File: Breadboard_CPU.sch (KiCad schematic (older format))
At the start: 20 parts, among them Q5 Q_NPN_CBE, SW3 RESET

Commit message: Pre non-interrupt split
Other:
- moved on the sheet: D14, D15, D16, D17, D18, D19, D20, D21, Q5, R100, R101, R102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

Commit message: Replaced all broken schematics with the up-to-date versions.  Some symbols missing.  This version will be the one created IRL except for the carry flag.
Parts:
- added R110: 10k, symbol Breadboard_CPU-rescue:R-Device
- D101: renamed from D14; symbol Device:LED -> Breadboard_CPU-rescue:LED-Device
- D102: renamed from D15; symbol Device:LED -> Breadboard_CPU-rescue:LED-Device
- D103: renamed from D16; symbol Device:LED -> Breadboard_CPU-rescue:LED-Device
- D104: renamed from D17; symbol Device:LED -> Breadboard_CPU-rescue:LED-Device
- D105: renamed from D18; symbol Device:LED -> Breadboard_CPU-rescue:LED-Device
- D106: renamed from D19; symbol Device:LED -> Breadboard_CPU-rescue:LED-Device
- D107: renamed from D20; symbol Device:LED -> Breadboard_CPU-rescue:LED-Device
- D108: renamed from D21; symbol Device:LED -> Breadboard_CPU-rescue:LED-Device
- Q101: renamed from Q5; value Q_NPN_CBE -> 2N2222; symbol Device:Q_NPN_CBE -> Breadboard_CPU-rescue:Q_NPN_CBE-Device
- R101: renamed from R99; symbol Device:R -> Breadboard_CPU-rescue:R-Device
- R102: renamed from R100; symbol Device:R -> Breadboard_CPU-rescue:R-Device
- R103: renamed from R101; symbol Device:R -> Breadboard_CPU-rescue:R-Device
- R104: renamed from R102; symbol Device:R -> Breadboard_CPU-rescue:R-Device
- R105: renamed from R103; symbol Device:R -> Breadboard_CPU-rescue:R-Device
- R106: renamed from R104; symbol Device:R -> Breadboard_CPU-rescue:R-Device
- R107: renamed from R105; symbol Device:R -> Breadboard_CPU-rescue:R-Device
- R108: renamed from R106; symbol Device:R -> Breadboard_CPU-rescue:R-Device
- R109: renamed from R29; symbol Device:R -> Breadboard_CPU-rescue:R-Device
- R111: renamed from R30; symbol Device:R -> Breadboard_CPU-rescue:R-Device
- SW101: renamed from SW3; symbol Switch:SW_Push -> Breadboard_CPU-rescue:SW_Push-Switch
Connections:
- net Clock Module/HALT_C renamed RST
- net RST: now also R110.1; no longer Q101.2 (B)
- net Control Unit Module/~RST renamed ~RST
- new net: Q101.2 (B), R110.2
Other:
- note added: "Annotation Key:\n100's: Main Sheet\n200's: Power Module\n300's: Clock Module\n400's: Memory Module\n500's: ALU Module\n600's: Control Unit\n700's: Registers Module\n800's PC Module"
- moved on the sheet: D101, D102, D103, D104, D105, D106, D107, D108, R101, R102, R103, R104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

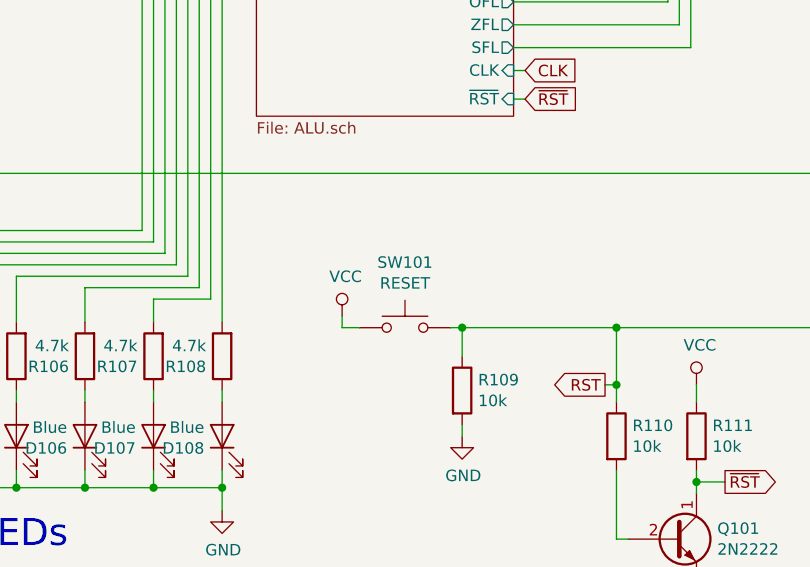
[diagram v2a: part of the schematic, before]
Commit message: Fixed CFL timing violation bug.  TOFIX: move away from rescue .lib symbols and fix the 2x 4:1 mux symbol.
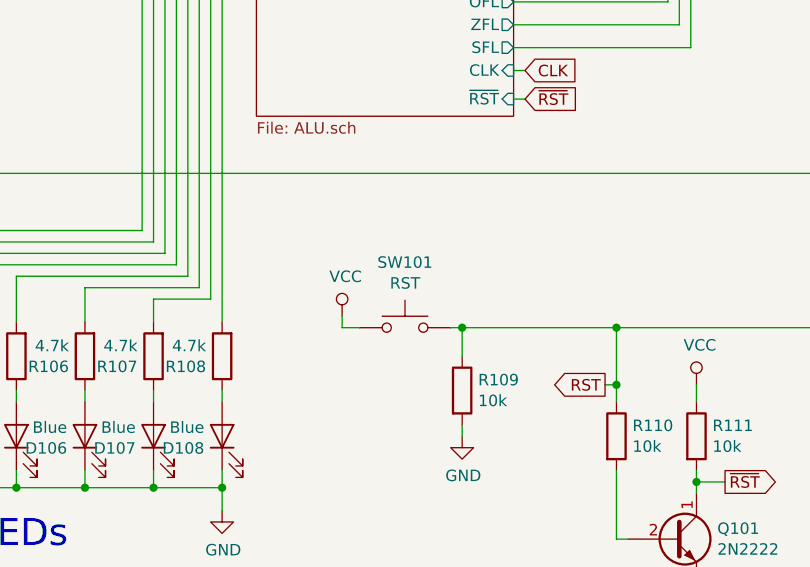
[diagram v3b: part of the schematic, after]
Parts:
- SW101: value RESET -> RST
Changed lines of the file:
@@
 P 5525 9350
 F 0 "SW101" H 5525 9635 50  0000 C CNN
-F 1 "RESET" H 5525 9544 50  0000 C CNN
+F 1 "RST" H 5525 9544 50  0000 C CNN
 F 2 "" H 5525 9550 50  0001 C CNN
 F 3 "~" H 5525 9550 50  0001 C CNN

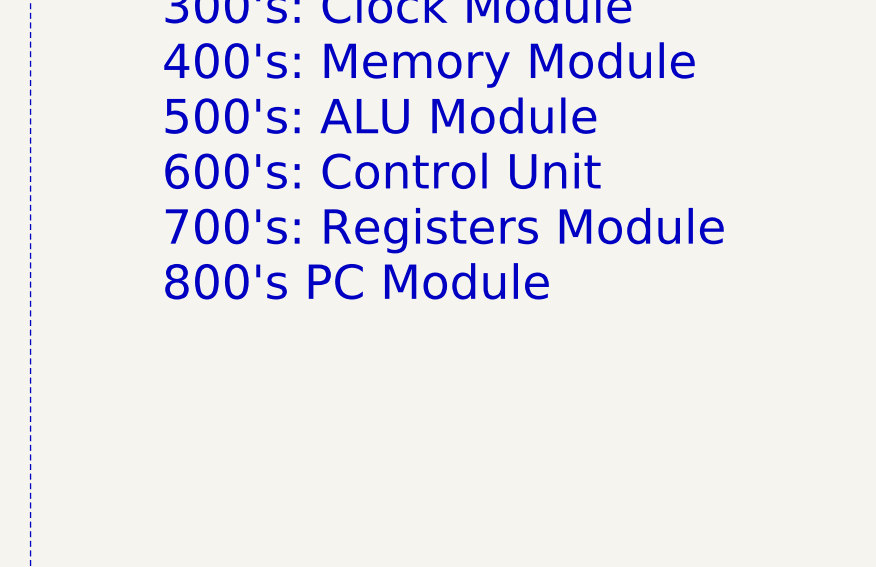
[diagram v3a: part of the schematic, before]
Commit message: Rearranged some generic logic gates in ALU to match physical net connections on the breadboard.
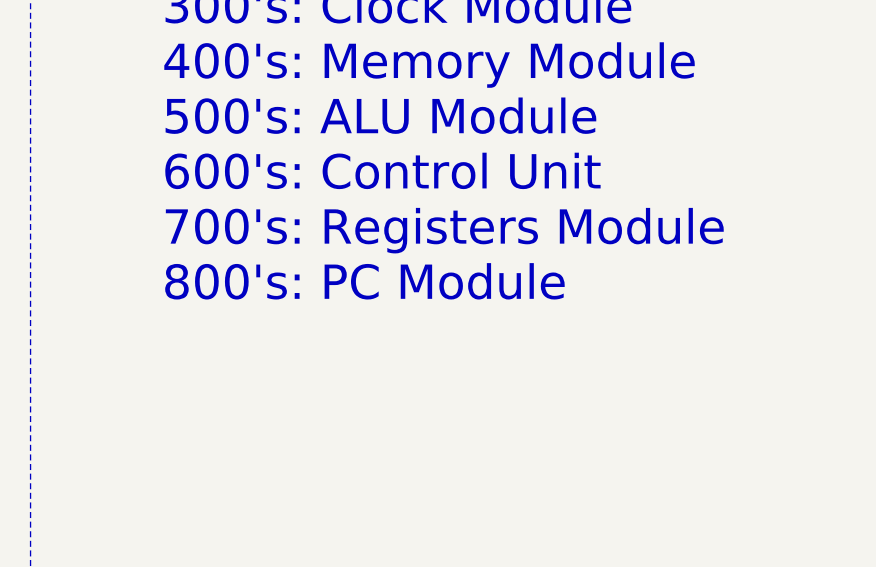
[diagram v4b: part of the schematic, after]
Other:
- note added: "Annotation Key:\n100's: Main Sheet\n200's: Power Module\n300's: Clock Module\n400's: Memory Module\n500's: ALU Module\n600's: Control Unit\n700's: Registers Module\n800's: PC Module"
- note removed: "Annotation Key:\n100's: Main Sheet\n200's: Power Module\n300's: Clock Module\n400's: Memory Module\n500's: ALU Module\n600's: Control Unit\n700's: Registers Module\n800's PC Module"
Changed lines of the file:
@@
 $EndSheet
 Text Notes 10925 5500 0    150  ~ 0
-Annotation Key:\n100's: Main Sheet\n200's: Power Module\n300's: Clock Module\n400's: Memory Module\n500's: ALU Module\n600's: Control Unit\n700's: Registers Module\n800's PC Module
+Annotation Key:\n100's: Main Sheet\n200's: Power Module\n300's: Clock Module\n400's: Memory Module\n500's: ALU Module\n600's: Control Unit\n700's: Registers Module\n800's: PC Module
 $Sheet
 S 3300 5825 900  900

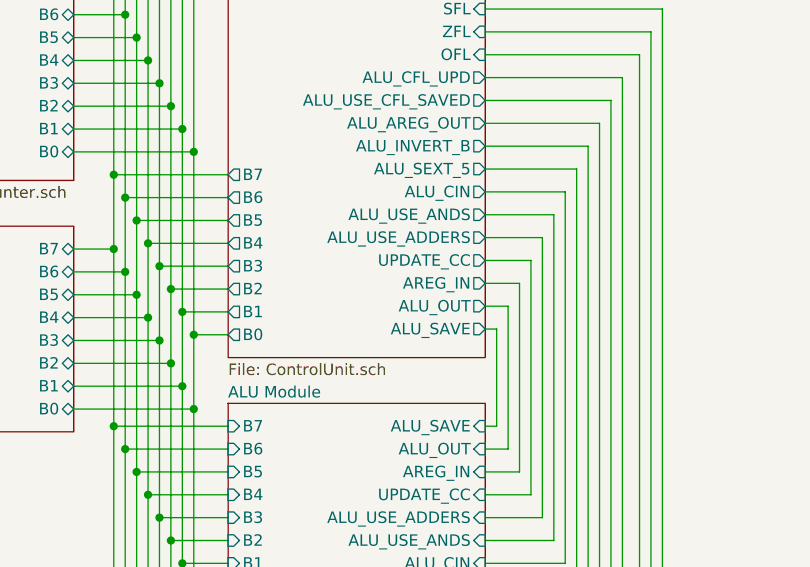
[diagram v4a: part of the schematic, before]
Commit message: Libraries re-imported.  Using rescue symbols still.  Adjusted multi-byte registers to use low-byte first.. applied this convention to all multi-byte registers for consistency.
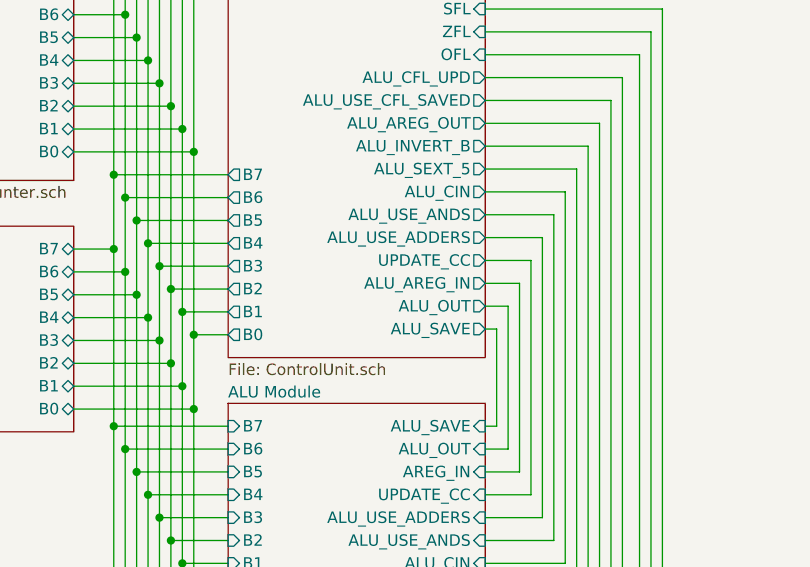
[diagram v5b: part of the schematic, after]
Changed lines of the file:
@@
 F20 "B1" O L 4875 6200 50
 F21 "B0" O L 4875 6300 50
-F22 "AREG_IN" O R 6000 6075 50
-F23 "UPDATE_CC" O R 6000 5975 50
-F24 "TR_HALT" O R 6000 4325 50
-F25 "OFL" I R 6000 5075 50
-F26 "ZFL" I R 6000 4975 50
-F27 "SFL" I R 6000 4875 50
-F28 "~PC_OUT" O R 6000 3650 50
-F29 "~PC_IN" O R 6000 3450 50
-F30 "~MEM_OUT" O R 6000 4175 50
-F31 "SP_INC" O L 4875 3325 50
-F32 "SP_DEC" O L 4875 3425 50
-F33 "ALU_USE_ADDERS" O R 6000 5875 50
-F34 "ALU_USE_ANDS" O R 6000 5775 50
-F35 "ALU_CIN" O R 6000 5675 50
-F36 "ALU_SEXT_5" O R 6000 5575 50
-F37 "ALU_INVERT_B" O R 6000 5475 50
-F38 "ALU_USE_CFL_SAVED" O R 6000 5275 50
-F39 "PC_IN" O R 6000 3550 50
-F40 "PC_OUT" O R 6000 3750 50
-F41 "ALU_OUT" O R 6000 6175 50
-F42 "ALU_AREG_OUT" O R 6000 5375 50
-F43 "~SP_IN" O R 6000 2825 50
-F44 "~SP_OUT" O R 6000 3025 50
-F45 "SP_OUT" O R 6000 3125 50
-F46 "SP_IN" O R 6000 2925 50
-F47 "ALU_CFL_UPD" O R 6000 5175 50
+F22 "UPDATE_CC" O R 6000 5975 50
+F23 "TR_HALT" O R 6000 4325 50
+F24 "OFL" I R 6000 5075 50
+F25 "ZFL" I R 6000 4975 50
+F26 "SFL" I R 6000 4875 50
+F27 "~PC_OUT" O R 6000 3650 50
+F28 "~PC_IN" O R 6000 3450 50
+F29 "~MEM_OUT" O R 6000 4175 50
+F30 "SP_INC" O L 4875 3325 50
+F31 "SP_DEC" O L 4875 3425 50
+F32 "ALU_USE_ADDERS" O R 6000 5875 50
+F33 "ALU_USE_ANDS" O R 6000 5775 50
+F34 "ALU_CIN" O R 6000 5675 50
+F35 "ALU_SEXT_5" O R 6000 5575 50
+F36 "ALU_INVERT_B" O R 6000 5475 50
+F37 "ALU_USE_CFL_SAVED" O R 6000 5275 50
+F38 "PC_IN" O R 6000 3550 50
+F39 "PC_OUT" O R 6000 3750 50
+F40 "ALU_OUT" O R 6000 6175 50
+F41 "ALU_AREG_OUT" O R 6000 5375 50
+F42 "~SP_IN" O R 6000 2825 50
+F43 "~SP_OUT" O R 6000 3025 50
+F44 "SP_OUT" O R 6000 3125 50
+F45 "SP_IN" O R 6000 2925 50
+F46 "ALU_CFL_UPD" O R 6000 5175 50
+F47 "ALU_AREG_IN" O R 6000 6075 50
 $EndSheet
 Wire Wire Line
